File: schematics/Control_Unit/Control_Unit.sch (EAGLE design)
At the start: 121 parts, among them IC10 74HC74N, IC103 74HC373N, IC11 74HC74N, IC12 74AC08N, IC126 74AC157N, IC128 74AC08N, IC129 74AC08N, IC13 74AC08N, IC14 74HC74N, IC15 74HC74N, IC16 74AC08N, IC164 74HC174N, IC165 74HC174N, IC166 74HC174N, IC167 74HC174N, IC168 74HCT32N, IC169 74HCT32N, IC17 74HC193N, IC172 74HCT32N, IC173 74HCT32N, IC174 74HCT32N, IC175 74HC193N, IC176 74HC193N, IC177 74HC193N, IC178 74HC193N, IC179 74HC193N, IC18 74AC08N, IC180 74HC193N, IC181 74HC193N, IC182 74HC193N, IC19 74AC08N, IC190 74HCT32N, IC191 74HCT32N, IC20 74AC08N, IC21 74AC08N, IC22 74HCT32N, IC23 74HCT08N, IC24 74HCT08N, IC25 74HCT32N, IC26 74HCT08N, IC27 74HCT08N, IC28 74HCT08N, IC29 74HCT08N, IC3 74HC151N, IC30 74HCT08N, IC32 74HCT32N, IC34 74HCT08N, IC35 74HCT04N, IC36 CY62256LL-PC, IC37 74HCT04N, IC39 74HCT08N, IC4 74HC174N, IC40 74HCT04N, IC41 74HCT08N, IC42 74HC373N, IC43 74HCT04N, IC44 74HCT04N, IC45 74HC193N, IC46 74ACT157N, IC47 74HCT04N, IC49 74AC86N, IC5 74HC174N, IC50 74HC174N, IC52 74HCT32N, IC55 74HCT32N, IC56 74HC151N, IC57 74HC151N, IC58 74HC151N, IC59 74HC151N, IC6 74HC174N, IC60 74HC151N, IC61 74HC151N, IC62 74HC174N, IC63 74HCT32N, IC64 74HCT32N, IC65 74HC174N, IC66 74HC174N, IC67 74HC174N, IC68 74HC174N, IC69 74HC174N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

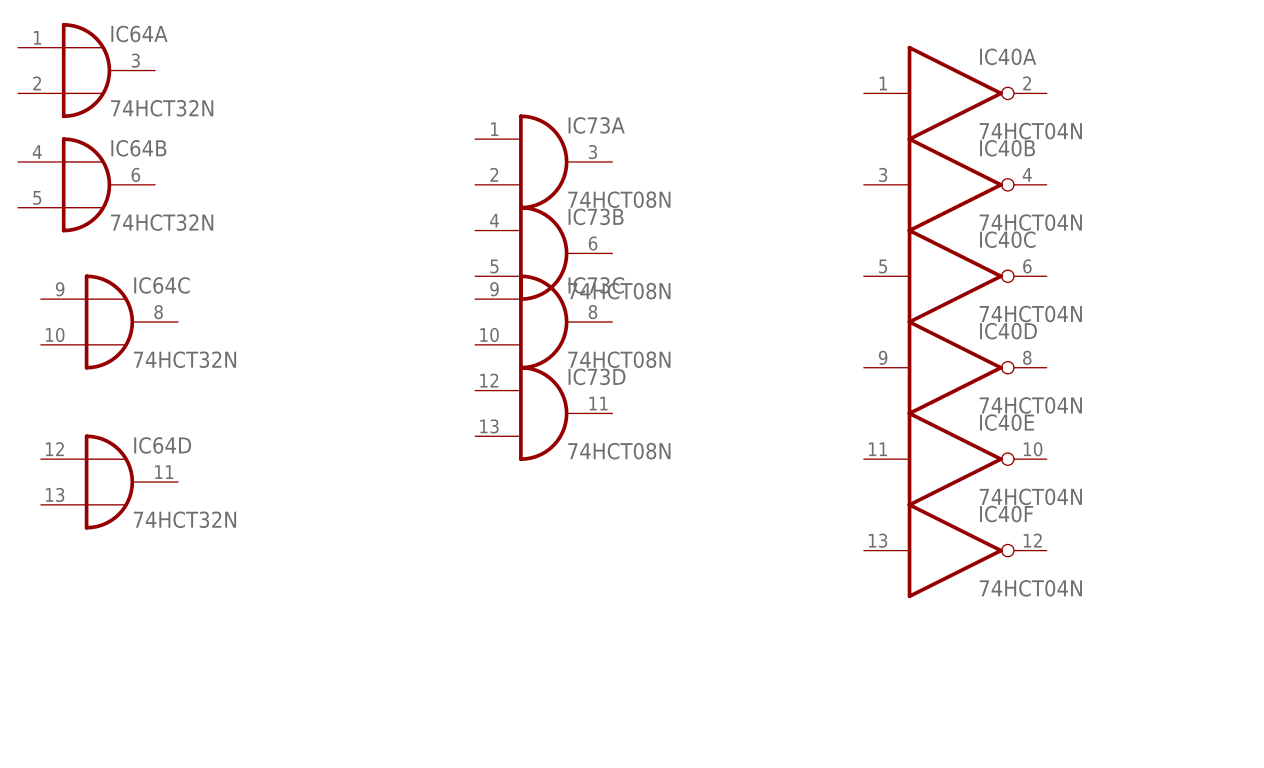
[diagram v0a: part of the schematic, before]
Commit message: scale down the *brd. started the layout
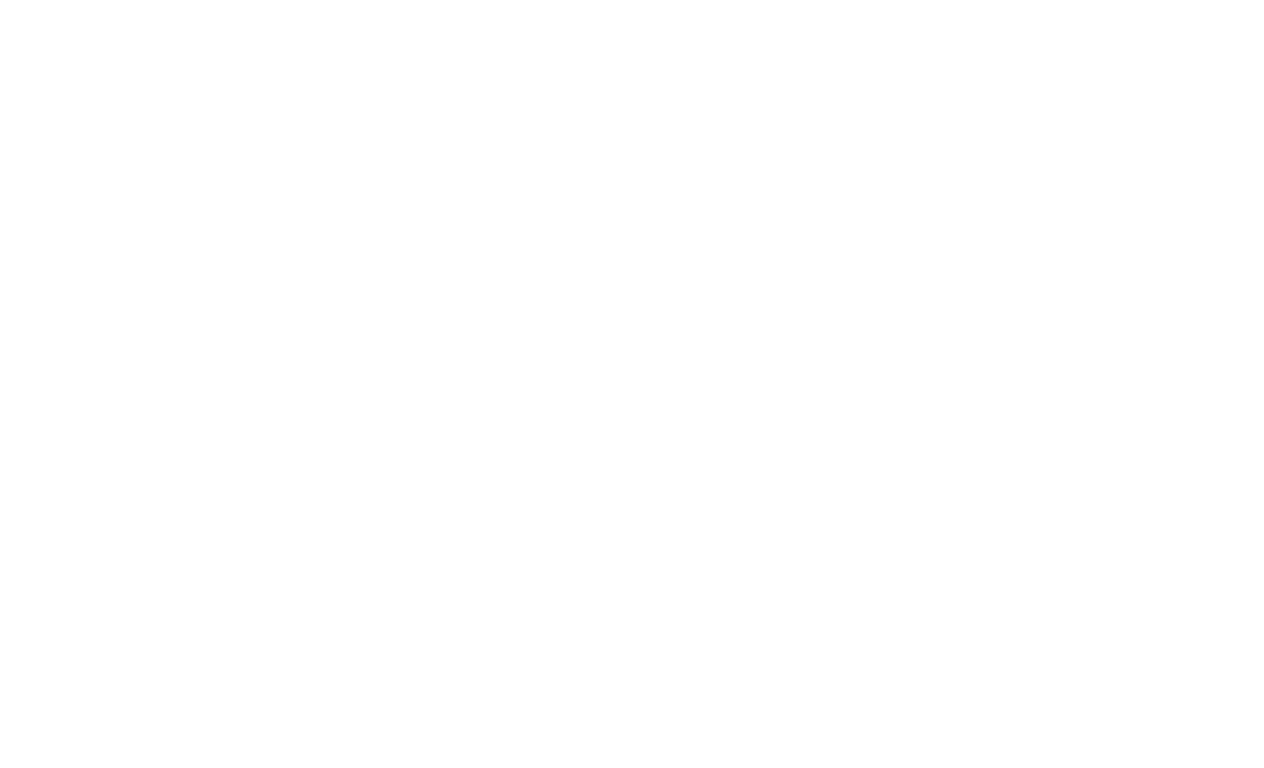
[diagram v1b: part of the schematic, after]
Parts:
- removed IC40: 74HCT04N, 74xx-eu:74HCT04N
- removed IC64: 74HCT32N, 74xx-eu:74HCT32N
- removed IC73: 74HCT08N, 74xx-eu:74HCT08N
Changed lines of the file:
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@@
 <part name="IC55" library="74xx-eu" deviceset="74*32" device="N" technology="HCT"/>
 <part name="IC63" library="74xx-eu" deviceset="74*32" device="N" technology="HCT"/>
-<part name="IC64" library="74xx-eu" deviceset="74*32" device="N" technology="HCT"/>
 <part name="IC27" library="74xx-eu" deviceset="74*08" device="N" technology="HCT"/>
 <part name="IC28" library="74xx-eu" deviceset="74*08" device="N" technology="HCT"/>
@@
 <part name="IC39" library="74xx-eu" deviceset="74*08" device="N" technology="HCT"/>
 <part name="IC41" library="74xx-eu" deviceset="74*08" device="N" technology="HCT"/>
-<part name="IC73" library="74xx-eu" deviceset="74*08" device="N" technology="HCT"/>
 <part name="IC76" library="74xx-eu" deviceset="74*08" device="N" technology="HCT"/>
 <part name="IC35" library="74xx-eu" deviceset="74*04" device="N" technology="HCT"/>
 <part name="IC37" library="74xx-eu" deviceset="74*04" device="N" technology="HCT"/>
-<part name="IC40" library="74xx-eu" deviceset="74*04" device="N" technology="HCT"/>
 <part name="IC43" library="74xx-eu" deviceset="74*04" device="N" technology="HCT"/>
 <part name="IC44" library="74xx-eu" deviceset="74*04" device="N" technology="HCT"/>
@@
 <text x="-419.1" y="-218.44" size="1.778" layer="91">PUSH</text>
 <text x="-419.1" y="-256.54" size="1.778" layer="91">POP</text>
-<frame x1="-957.58" y1="-711.2" x2="1272.54" y2="693.42" columns="7" rows="5" layer="91"/>
 <text x="-708.66" y="22.86" size="12.7" layer="91">Opcode Instruction Decoder</text>
 <text x="1023.62" y="330.2" size="1.778" layer="91">RAM W24129AK</text>
@@
 <instance part="IC63" gate="C" x="1112.52" y="-233.68"/>
 <instance part="IC63" gate="D" x="952.5" y="205.74"/>
-<instance part="IC64" gate="A" x="-876.3" y="655.32"/>
-<instance part="IC64" gate="B" x="-876.3" y="642.62"/>
-<instance part="IC64" gate="C" x="-873.76" y="627.38"/>
-<instance part="IC64" gate="D" x="-873.76" y="609.6"/>
 <instance part="IC27" gate="A" x="-294.64" y="-162.56"/>
 <instance part="IC27" gate="B" x="-167.64" y="-162.56"/>
@@
 <instance part="IC41" gate="C" x="-551.18" y="502.92"/>
 <instance part="IC41" gate="D" x="-551.18" y="490.22"/>
-<instance part="IC73" gate="A" x="-825.5" y="645.16"/>
-<instance part="IC73" gate="B" x="-825.5" y="635"/>
-<instance part="IC73" gate="C" x="-825.5" y="627.38"/>
-<instance part="IC73" gate="D" x="-825.5" y="617.22"/>
 <instance part="IC76" gate="A" x="-269.24" y="439.42"/>
 <instance part="IC76" gate="B" x="-269.24" y="426.72"/>
@@
 <instance part="IC37" gate="E" x="1153.16" y="264.16"/>
 <instance part="IC37" gate="F" x="1163.32" y="248.92"/>
-<instance part="IC40" gate="A" x="-779.78" y="652.78"/>
-<instance part="IC40" gate="B" x="-779.78" y="642.62"/>
-<instance part="IC40" gate="C" x="-779.78" y="632.46"/>
-<instance part="IC40" gate="D" x="-779.78" y="622.3"/>
-<instance part="IC40" gate="E" x="-779.78" y="612.14"/>
-<instance part="IC40" gate="F" x="-779.78" y="601.98"/>
 <instance part="IC43" gate="A" x="-505.46" y="284.48"/>
 <instance part="IC43" gate="B" x="-505.46" y="271.78"/>

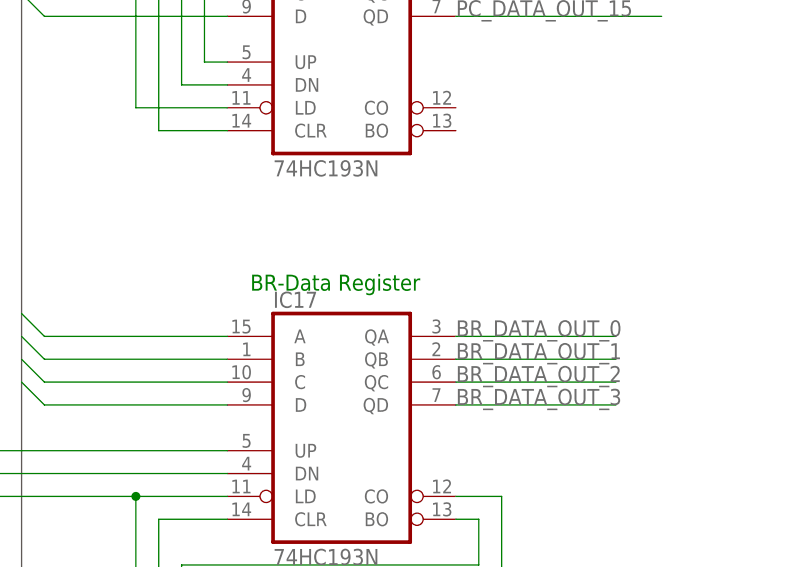
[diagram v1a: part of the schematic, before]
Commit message: improve arch-design:
rename BR register to PTR,
rename COUNT_BR to PTR_ADD
allow ofsets for PTR_ADD
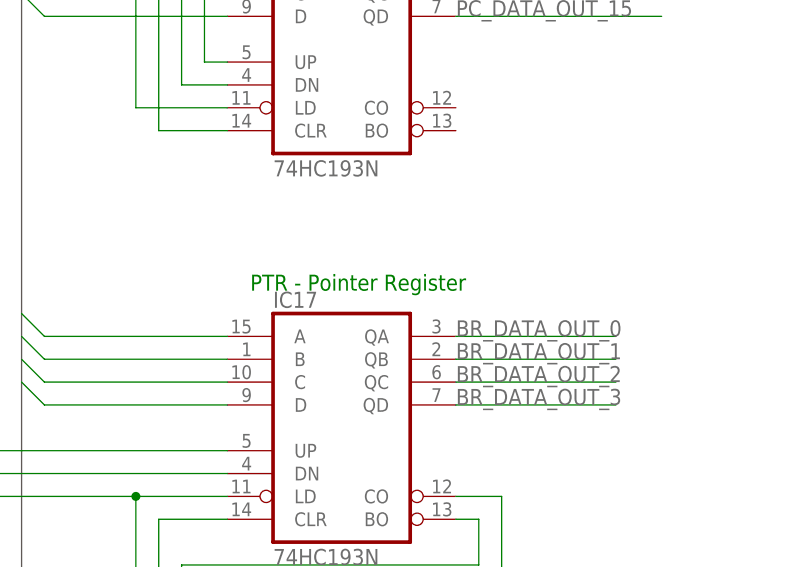
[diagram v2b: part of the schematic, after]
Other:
- note added: "PTR - Pointer Register"
- note removed: "BR-Data Register"
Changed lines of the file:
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@@
 <text x="1168.4" y="330.2" size="5.08" layer="91">StackMemory</text>
 <text x="-264.16" y="480.06" size="2.54" layer="91">Multiplexer to use either Output_REGX or INPUT_REGX for the output selecter</text>
-<text x="325.12" y="-208.28" size="1.778" layer="91">BR-Data Register</text>
+<text x="325.12" y="-208.28" size="1.778" layer="91">PTR - Pointer Register</text>
 <text x="-419.1" y="-335.28" size="1.778" layer="91">COUNT_BR</text>
 <text x="-444.5" y="-337.82" size="1.778" layer="91">UP</text>

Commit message: implement SET_PTR instruction
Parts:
- removed IC45: 74HC193N, custom_parts:74HC193N
- added IC1, IC2: 74HC174N, 74xx-eu:74HC174N
- added IC31: 74HCT08N, 74xx-eu:74HCT08N
- added IC33: 74HCT04N, 74xx-eu:74HCT04N
- IC17: value 74HC193N -> 74HCT32N; device custom_parts:74HC193N -> 74xx-eu:74HCT32N
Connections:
- net BR_DATA_OUT_10 renamed PTR_DATA_OUT_10
- net BR_DATA_OUT_11 renamed PTR_DATA_OUT_11
- net BR_DATA_OUT_12 renamed PTR_DATA_OUT_12
- net BR_DATA_OUT_13 renamed PTR_DATA_OUT_13
- net BR_DATA_OUT_14 renamed PTR_DATA_OUT_14
- net BR_DATA_OUT_15 renamed PTR_DATA_OUT_15
- net BR_DATA_OUT_8 renamed PTR_DATA_OUT_8
- net BR_DATA_OUT_9 renamed PTR_DATA_OUT_9
- net BR_HIGH_LOAD_INPUT_NOT renamed PTR_H_LOAD_INPUT_NOT
- net BR_TO_ABUS/!PC_TO_ABUS renamed PTR_TO_ABUS/!PC_TO_ABUS
- net CONNECT_REG_TO_DBUS_BR renamed CONNECT_REG_TO_DBUS_PTR
- net FILL_BR_HIGH_BR renamed FILL_PTR_H_SET_PTR
- net FILL_BR_LOW_BR renamed FILL_PTR_L_SET_PTR
- net TABLE_B_INPUT_BR_LOW renamed TABLE_B_INPUT_PTR_L
- net WRITE_REGB_TO_DBUS_BR renamed WRITE_REGB_TO_DBUS_SET_PTR
- removed net BR_COUNT_DOWN: IC17A.DN, IC44D.O
- removed net BR_COUNT_UP: IC17A.UP, IC44C.O
- removed net BR_DATA_OUT_0: IC17A.QA, IC61A.D5, IC86A.1A
- removed net BR_DATA_OUT_1: IC17A.QB, IC60A.D5, IC86A.2A
- removed net BR_DATA_OUT_2: IC17A.QC, IC59A.D5, IC86A.3A
- removed net BR_DATA_OUT_3: IC17A.QD, IC58A.D5, IC86A.4A
- removed net BR_DATA_OUT_4: IC45A.QA, IC57A.D5, IC87A.1A
- removed net BR_DATA_OUT_5: IC45A.QB, IC56A.D5, IC87A.2A
- removed net BR_DATA_OUT_6: IC3A.D5, IC45A.QC, IC87A.3A
- removed net BR_DATA_OUT_7: IC45A.QD, IC87A.4A, IC9A.D5
- removed net BR_LOW_LOAD_INPUT_NOT: IC17A.LD, IC43A.O, IC45A.LD
- removed net DATA10: IC17A.C, IC82A.C
- removed net DATA11: IC17A.D, IC82A.D
- removed net DATA12: IC45A.A, IC83A.A
- removed net DATA13: IC45A.B, IC83A.B
- removed net DATA14: IC45A.C, IC83A.C
- removed net DATA15: IC45A.D, IC83A.D
- removed net DATA8: IC17A.A, IC82A.A
- removed net DATA9: IC17A.B, IC82A.B
- removed net N$101: IC45A.BO, IC82A.DN
- removed net N$161: IC21C.O, IC29A.I0, IC29C.I0
- removed net N$195: IC21B.O, IC24D.I1, IC26A.I1, IC26B.I1, IC26C.I1
- removed net N$227: IC29B.O, IC44C.I
- removed net N$228: IC29C.O, IC29D.I1
- removed net N$233: IC29D.O, IC44D.I
- removed net N$239: IC179A.CLR, IC180A.CLR, IC181A.CLR, IC182A.CLR
- new net N$82: IC17B.O, IC29C.I1, IC33A.I
- new net N$96: IC20C.O
- new net N$97: IC20D.O, IC24D.I1, IC26A.I1, IC26B.I1, IC26C.I1
- new net N$98: IC21A.O
- new net N$99: IC21C.O
- new net PTR_DATA_OUT_0: IC1A.Q1, IC61A.D5, IC86A.1A
- new net PTR_DATA_OUT_1: IC1A.Q2, IC60A.D5, IC86A.2A
- new net PTR_DATA_OUT_2: IC1A.Q3, IC59A.D5, IC86A.3A
- new net PTR_DATA_OUT_3: IC1A.Q4, IC58A.D5, IC86A.4A
- new net PTR_DATA_OUT_4: IC1A.Q5, IC57A.D5, IC87A.1A
- new net PTR_DATA_OUT_5: IC1A.Q6, IC56A.D5, IC87A.2A
- new net PTR_DATA_OUT_6: IC2A.Q1, IC3A.D5, IC87A.3A
- new net PTR_DATA_OUT_7: IC2A.Q2, IC87A.4A, IC9A.D5
- new net PTR_HIGH_COUNT_DOWN: IC82A.DN
- new net PTR_HIGH_COUNT_UP: IC82A.UP
- new net PTR_L_LOAD_INPUT_NOT: IC1A.CLK, IC2A.CLK, IC43A.O
- net DATA0: now also IC1A.D1
- net DATA1: now also IC1A.D2
- net DATA2: now also IC1A.D3
- net DATA3: now also IC1A.D4
- net DATA4: now also IC1A.D5
- net DATA5: now also IC1A.D6
- net DATA6: now also IC2A.D1
- net DATA7: now also IC2A.D2
- net GND: now also IC179A.CLR, IC180A.CLR, IC181A.CLR, IC182A.CLR, IC1A.CLR, IC2A.CLR, IC2A.D3, IC2A.D4, IC2A.D5, IC2A.D6, IC82A.A, IC82A.B, IC82A.C, IC82A.D; no longer IC17A.CLR, IC45A.CLR
- net INPUT_REG0: now also IC17B.I0
- net N$100: now also IC21B.O; no longer IC17A.BO, IC45A.DN
- net N$112: no longer IC20B.O
- net N$129: no longer IC20D.O
- net N$13: no longer IC20C.O
- net N$148: no longer IC21A.O
- net N$15: now also IC20B.O, IC31C.I1; no longer IC17A.CO, IC45A.UP
- net N$200: now also IC29C.O; no longer IC174C.O
- net N$21: now also IC31C.O; no longer IC29A.O, IC29B.I1
- net N$22: now also IC31C.I0, IC33A.O; no longer IC29C.I1, IC47E.O
- net N$7: now also IC174C.O, IC29C.I0; no longer IC45A.CO, IC82A.UP
- net OPCODE_4: no longer IC29A.I1, IC47E.I
- net OUTPUT_REG0_JMP: now also IC17B.I1
- net STATE_1: no longer IC29B.I0, IC29D.I0
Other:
- note added: "ADD_PTR"
- note added: "Check whether offset jmp"
- note added: "JMP (with offset)"
- note added: "SET_PTR"
- note removed: "COUNT_BR"
- note removed: "DOWN"
- note removed: "SET_BR"
- note removed: "UP"
- moved on the sheet: IC129A, IC129B, IC129C, IC129D, IC169A, IC169D, IC172A, IC172B, IC172C, IC172D, IC173A, IC173B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

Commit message: schematic: implemented JMP offset instruction.
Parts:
- added IC38, IC45, IC48, IC51, IC53, IC85, IC90, IC92: 74HCT08N, 74xx-eu:74HCT08N
- added IC40, IC54, IC64, IC70, IC73, IC80, IC81, IC84, IC94, IC99: 74HCT32N, 74xx-eu:74HCT32N
- added IC77, IC79: 74ACT157N, 74xx-eu:74ACT157N
- added IC91, IC93, IC95, IC97, IC98: 74HCT04N, 74xx-eu:74HCT04N
- added JP8: (no value), pinhead:PINHD-1X4
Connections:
- removed net LATCH_ALU_OUTPUT_ALU: IC42A.ENC, IC75C.O
- removed net N$243: IC180A.BO, IC181A.DN
- new net ALU_CARRY_OUT: IC92D.I0, JP8.4
- new net FILL_PC_L_JMP_O: IC51D.O, IC81B.I1, IC84B.I1
- new net LATCH_ALU_INPUT_B_ALU: IC54D.I0, IC73B.I0, IC75A.O
- new net LATCH_ALU_INPUT_B_JMP_O: IC40A.I0, IC45D.O, IC73B.I1
- new net N$101: IC80B.I1
- new net N$108: IC103A.2D, IC77A.2Y
- new net N$109: IC38C.O, IC40A.I1
- new net N$110: IC54D.I1, IC78D.O
- new net N$114: IC103A.3D, IC77A.3Y
- new net N$115: IC77A.!A!/B, IC79A.!A!/B, IC80B.O
- new net N$116: IC103A.4D, IC77A.4Y
- new net N$124: IC103A.5D, IC79A.1Y
- new net N$125: IC103A.6D, IC79A.2Y
- new net N$127: IC103A.7D, IC79A.3Y
- new net N$128: IC90D.I0, IC91B.O
- new net N$132: IC31C.O, IC38C.I1, IC45D.I1, IC48D.I1, IC51D.I1, IC53D.I1
- new net N$133: IC181A.DN, IC98B.O
- new net N$134: IC103A.8D, IC79A.4Y
- new net N$135: IC35E.I, IC81B.O
- new net N$136: IC43C.I, IC84B.O
- new net N$137: IC53D.O, IC92D.I1
- new net N$138: IC180A.CO, IC93B.I
- new net N$139: IC85D.I1, IC90D.I1, IC92D.O
- new net N$140: IC180A.BO, IC97B.I
- new net N$141: IC94C.O, IC95B.I
- new net N$142: IC93B.O, IC94C.I0
- new net N$144: IC98B.I, IC99C.O
- new net N$145: IC97B.O, IC99C.I1
- new net PC_H_COUNT_DOWN_JMP_O: IC85D.O, IC99C.I0
- new net PC_H_COUNT_UP_JMP_O: IC90D.O, IC94C.I1
- new net WRITE_PC_L_ALU_LATCH_JMP_O: IC40A.O, IC80B.I0
- new net WRITE_REGB_TO_DBUS_ALU_JMP_O: IC48D.O
- new net WRITE_REG_TO_DBUS_JMP_O: IC64B.I0
- net DATA0: now also IC77A.1B; no longer IC103A.1D
- net DATA1: now also IC77A.2B; no longer IC103A.2D
- net DATA2: now also IC77A.3B; no longer IC103A.3D
- net DATA3: now also IC77A.4B; no longer IC103A.4D
- net DATA4: now also IC79A.1B; no longer IC103A.5D
- net DATA5: now also IC79A.2B; no longer IC103A.6D
- net DATA6: now also IC79A.3B; no longer IC103A.7D
- net DATA7: now also IC79A.4B; no longer IC103A.8D
- net FILL_REGISTER_ALU/ALU_TO_DBUS: now also IC81B.I0; no longer IC35E.I
- net GND: now also IC77A.G, IC79A.G
- net INPUT_REG0: no longer IC190B.I0
- net IR_DATA_OUT_7: now also IC85D.I0, IC91B.I
- net LATCH_ALU_INPUT_B: now also IC73B.O; no longer IC75A.O
- net N$11: now also IC64B.O, IC70B.I1; no longer IC190B.O, IC44A.I
- net N$14: now also IC42A.ENC
- net N$17: now also IC103A.1D, IC77A.1Y; no longer IC28B.O, IC28C.I1, IC28D.I1
- net N$2: now also IC52D.O, IC70B.I0; no longer IC28B.I0, IC44A.O
- net N$200: now also IC28C.I1, IC28D.I1; no longer IC28B.I1
- net N$21: now also IC64B.I1; no longer IC31C.O
- net N$240: now also IC95B.O; no longer IC180A.CO
- net N$47: no longer IC75C.I1
- net N$90: now also IC70B.O; no longer IC52D.O
- net OUTPUT_REG0_JMP: no longer IC190B.I1
- net PC_DATA_OUT_0: now also IC77A.1A
- net PC_DATA_OUT_1: now also IC77A.2A
- net PC_DATA_OUT_2: now also IC77A.3A
- net PC_DATA_OUT_3: now also IC77A.4A
- net PC_DATA_OUT_4: now also IC79A.1A
- net PC_DATA_OUT_5: now also IC79A.2A
- net PC_DATA_OUT_6: now also IC79A.3A
- net PC_DATA_OUT_7: now also IC79A.4A
- net PC_LOW_LOAD_INPUT_JMP: now also IC84B.I0; no longer IC43C.I
- net STATE_1: now also IC38C.I0
- net STATE_2: now also IC45D.I0
- net STATE_3: now also IC48D.I0
- net STATE_4: now also IC51D.I0, IC75D.I0; no longer IC75C.I0
- net STATE_5: now also IC53D.I0; no longer IC75D.I0
- net WRITE_REG_TO_DBUS_ALU: now also IC54D.O; no longer IC78D.O
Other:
- note added: "Does this work? Is there enough time?"
- note added: "Probalby need to latch it!"
- note removed: "If opcode nibble is 0x00, JMP is done."
- moved on the sheet: IC103, IC35E, IC52D, IC75D, JP1, JP3

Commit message: implement PTR_ADD instruction. All instruction are now implemented!
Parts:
- added IC100, IC102, IC106, IC108, IC110, IC117, IC118, IC124: 74HCT32N, 74xx-eu:74HCT32N
- added IC101, IC104, IC107, IC109, IC111, IC112, IC113, IC114, IC125, IC127: 74HCT08N, 74xx-eu:74HCT08N
- added IC105, IC121, IC122, IC123, IC130: 74HCT04N, 74xx-eu:74HCT04N
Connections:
- net LATCH_ALU_INPUT_B renamed N$96
- removed net ALU_NR1_ENABLE: IC18A.O, IC191A.I0, JP3.1
- removed net ALU_NR2_ENABLE: IC18B.O, IC191A.I1, JP3.2
- removed net N$100: IC21B.O
- removed net N$31: IC21D.O
- removed net N$96 (its old number): IC20C.O
- removed net N$98: IC21A.O
- removed net N$99: IC21C.O
- removed net WRITE_REGB_TO_DBUS_ALU_JMP_O: IC48D.O
- new net ALU_NR1_ENABLE_ALU: IC117A.I0, IC18A.O, IC191A.I0
- new net ALU_NR1_ENABLE_JMP_O_PTR_ADD: IC117A.I1, IC127C.O
- new net ALU_NR2_ENABLE_ALU: IC118A.I0, IC18B.O, IC191A.I1
- new net ALU_NR2_ENABLE_JMP_O_PTR_ADD: IC118A.I1, IC125C.O
- new net FILL_PTR_L_PTR_ADD: IC109D.O, IC110B.I1
- new net LATCH_ALU_INPUT_B_PTR_ADD: IC102A.I0, IC104D.O, IC106B.I1
- new net N$143: IC100B.O, IC168B.I0
- new net N$147: IC110B.O, IC81B.I1
- new net N$149: IC101C.I1, IC104D.I1, IC107D.I1, IC109D.I1, IC111D.I1, IC124B.I1, IC20C.O
- new net N$151: IC101C.O, IC102A.I1
- new net N$152: IC106B.O, IC73B.I1
- new net N$153: IC111D.O, IC112D.I1
- new net N$155: IC100B.I0, IC108B.O
- new net N$158: IC114D.O, IC123B.I
- new net N$159: IC112D.O, IC113D.I1, IC114D.I1
- new net N$161: IC113D.I0, IC121B.O
- new net N$162: IC113D.O, IC122B.I
- new net N$164: IC127C.I0, IC130A.O
- new net N$166: IC124B.O, IC125C.I1, IC127C.I1
- new net N$167: IC118A.O, JP3.2
- new net N$202: IC117A.O, JP3.1
- new net WRITE_PTR_L_TO_DBUS_PTR_ADD: IC102A.O, IC64B.I1
- new net WRITE_REGB_TO_DBUS_JMP_O: IC108B.I1, IC48D.O
- new net WRITE_REGB_TO_DBUS_PTR_ADD: IC107D.O, IC108B.I0
- net ALU_CARRY_OUT: now also IC112D.I0
- net FILL_PC_L_JMP_O: now also IC110B.I0; no longer IC81B.I1
- net IR_DATA_OUT_7: now also IC114D.I0, IC121B.I, IC125C.I0, IC130A.I
- net LATCH_ALU_INPUT_B_JMP_O: now also IC106B.I0; no longer IC73B.I1
- net N$112: now also IC21A.O
- net N$129: now also IC21C.O
- net N$13: now also IC21B.O
- net N$148: now also IC21D.O
- net N$15: now also IC124B.I0
- net N$21: now also IC105E.I, IC63C.O; no longer IC64B.I1
- net PTR_HIGH_COUNT_DOWN: now also IC123B.O
- net PTR_HIGH_COUNT_UP: now also IC122B.O
- net REG1_ZERO: now also IC105E.O; no longer IC63C.O
- net STATE_1: now also IC101C.I0
- net STATE_2: now also IC104D.I0
- net STATE_3: now also IC107D.I0
- net STATE_4: now also IC109D.I0
- net STATE_5: now also IC111D.I0
- net WRITE_REGB_TO_DBUS_JMP: now also IC100B.I1; no longer IC168B.I0
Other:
- moved on the sheet: IC12A, IC12B, IC12C, IC12D, IC13A, IC13B, IC13C, IC13D, IC168B, IC168C, IC169A, IC16A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
